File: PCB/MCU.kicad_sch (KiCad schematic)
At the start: 15 parts, among them J200 2171790001, J201 2086-1104, U200 ESP32-S3-WROOM-1, U201 USBLC6-2SC6

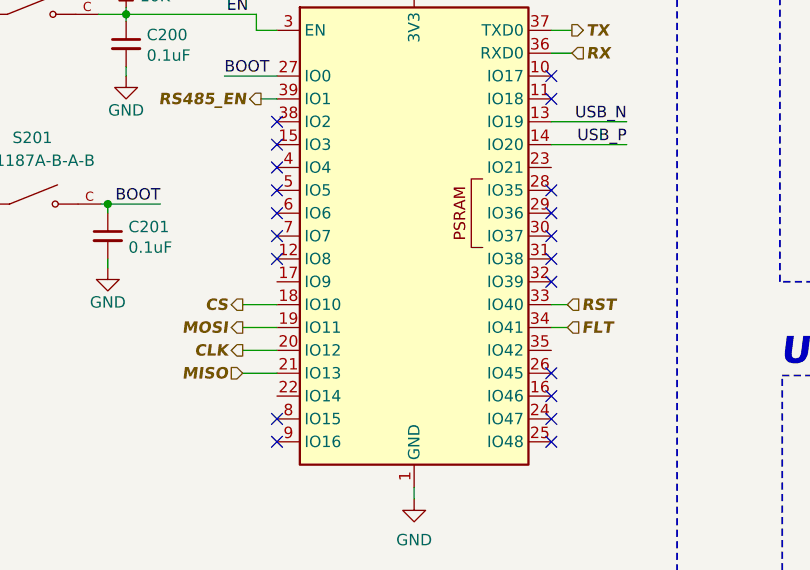
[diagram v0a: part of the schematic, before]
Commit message: pcb board terminada
Se termino:
- PCB board
- Labels de conectores y logo de la empresa
- Conexion WIZ850IO
- Conexion de MCU y WIZ850IO
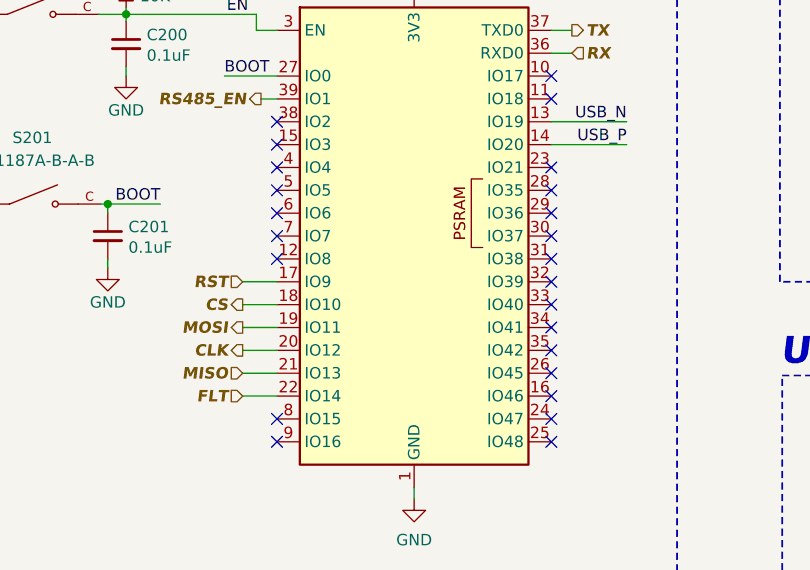
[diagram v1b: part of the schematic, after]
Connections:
- net FLT: now also U200.22 (IO14); no longer U200.34 (IO41)
- net RST: now also U200.17 (IO9); no longer U200.33 (IO40)
- no-connect marks 22 -> 26
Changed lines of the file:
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@@
+	)
+	(no_connect
+		(at 134.874 86.36)
 	)
 	(no_connect
@@
 	)
 	(no_connect
+		(at 134.874 106.68)
+	)
+	(no_connect
 		(at 104.394 96.52)
 	)
@@
 	)
 	(no_connect
+		(at 134.874 104.14)
+	)
+	(no_connect
 		(at 134.874 96.52)
 	)
 	(no_connect
+		(at 134.874 101.6)
+	)
+	(no_connect
 		(at 134.874 116.84)
 	)
@@
 	(wire
 		(pts
+			(xy 100.584 111.76) (xy 104.394 111.76)
+		)
+		(stroke
+			(width 0)
+			(type default)
+		)
+	)
+	(wire
+		(pts
 			(xy 242.57 64.516) (xy 246.126 64.516)
 		)
@@
 	(wire
 		(pts
-			(xy 134.874 101.6) (xy 136.652 101.6)
-		)
-		(stroke
-			(width 0)
-			(type default)
-		)
-	)
-	(wire
-		(pts
 			(xy 186.436 134.874) (xy 189.484 134.874)
 		)
@@
 	(wire
 		(pts
+			(xy 100.584 99.06) (xy 104.394 99.06)
+		)
+		(stroke
+			(width 0)
+			(type default)
+		)
+	)
+	(wire
+		(pts
 			(xy 178.562 76.708) (xy 180.848 76.708)
 		)
@@
 		(pts
 			(xy 134.874 81.28) (xy 143.256 81.28)
-		)
-		(stroke
-			(width 0)
-			(type default)
-		)
-	)
-	(wire
-		(pts
-			(xy 134.874 104.14) (xy 136.652 104.14)
 		)
 		(stroke
@@
 	(hierarchical_label "RST"
 		(shape input)
-		(at 136.652 101.6 0)
+		(at 100.584 99.06 180)
 		(fields_autoplaced yes)
 		(effects
@@
 				(italic yes)
 			)
-			(justify left)
+			(justify right)
 		)
 	)
@@
 	(hierarchical_label "FLT"
 		(shape input)
-		(at 136.652 104.14 0)
+		(at 100.584 111.76 180)
 		(fields_autoplaced yes)
 		(effects
@@
 				(italic yes)
 			)
-			(justify left)
-		)
-	)
+			(justify right)
+		)
+	)
